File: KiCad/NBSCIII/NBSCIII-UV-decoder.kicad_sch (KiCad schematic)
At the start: 29 parts, among them U2 4053, U3 LM324N

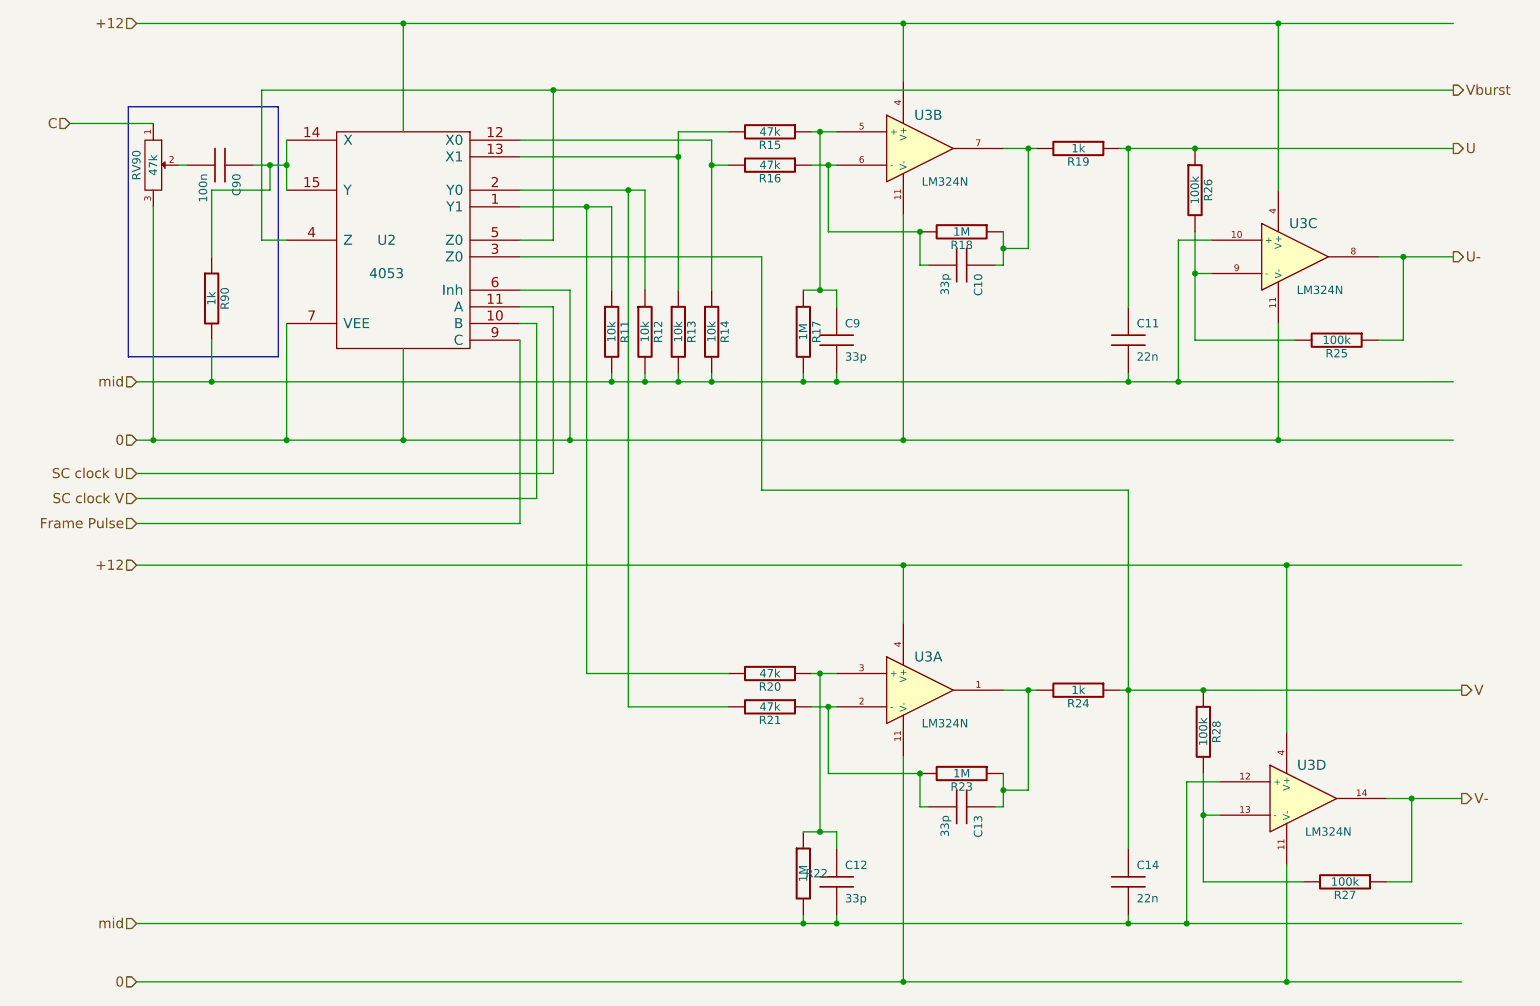
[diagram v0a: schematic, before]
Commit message: unrescue to Device:C
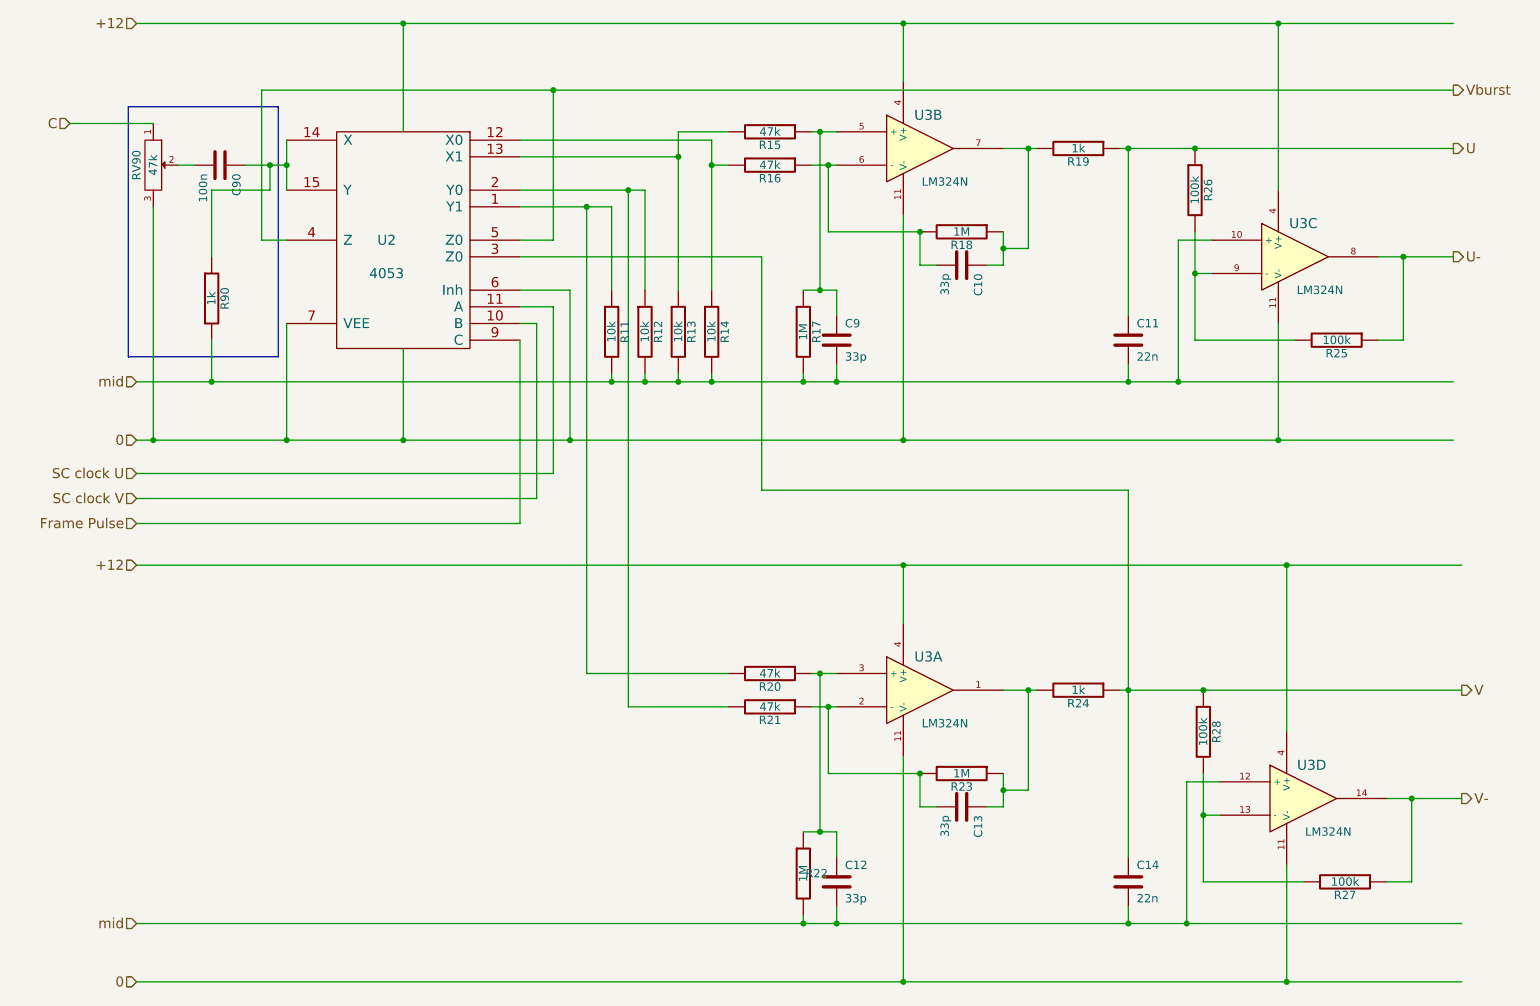
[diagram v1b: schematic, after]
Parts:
- C10, C11, C12, C13, C14, C9, C90: symbol NBSCIII-rescue:C -> Device:C
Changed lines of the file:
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@@
     (stroke (width 0) (type default) (color 0 0 0 0))
   )
-  (wire (pts (xy 41.91 45.72) (xy 40.64 45.72))
+  (wire (pts (xy 40.64 45.72) (xy 43.18 45.72))
     (stroke (width 0) (type default) (color 0 0 0 0))
   )
@@
     (stroke (width 0) (type default) (color 0 0 0 0))
   )
+  (wire (pts (xy 185.42 125.73) (xy 185.42 151.13))
+    (stroke (width 0) (type default) (color 0 0 0 0))
+  )
   (wire (pts (xy 140.97 147.32) (xy 138.43 147.32))
     (stroke (width 0) (type default) (color 0 0 0 0))
@@
     (stroke (width 0) (type default) (color 0 0 0 0))
   )
-  (wire (pts (xy 140.97 67.31) (xy 140.97 64.77))
-    (stroke (width 0) (type default) (color 0 0 0 0))
-  )
   (wire (pts (xy 111.76 49.53) (xy 111.76 64.77))
     (stroke (width 0) (type default) (color 0 0 0 0))
@@
     (stroke (width 0) (type default) (color 0 0 0 0))
   )
-  (wire (pts (xy 165.1 60.96) (xy 166.37 60.96))
+  (wire (pts (xy 185.42 43.18) (xy 185.42 68.58))
+    (stroke (width 0) (type default) (color 0 0 0 0))
+  )
+  (wire (pts (xy 163.83 60.96) (xy 166.37 60.96))
     (stroke (width 0) (type default) (color 0 0 0 0))
   )
@@
     (stroke (width 0) (type default) (color 0 0 0 0))
   )
-  (wire (pts (xy 185.42 67.31) (xy 185.42 43.18))
-    (stroke (width 0) (type default) (color 0 0 0 0))
-  )
   (wire (pts (xy 209.55 152.4) (xy 209.55 170.18))
     (stroke (width 0) (type default) (color 0 0 0 0))
@@
     (stroke (width 0) (type default) (color 0 0 0 0))
   )
-  (wire (pts (xy 165.1 143.51) (xy 166.37 143.51))
+  (wire (pts (xy 163.83 143.51) (xy 166.37 143.51))
     (stroke (width 0) (type default) (color 0 0 0 0))
   )
@@
     (stroke (width 0) (type default) (color 0 0 0 0))
   )
-  (wire (pts (xy 185.42 78.74) (xy 185.42 77.47))
+  (wire (pts (xy 185.42 76.2) (xy 185.42 78.74))
     (stroke (width 0) (type default) (color 0 0 0 0))
   )
@@
     (stroke (width 0) (type default) (color 0 0 0 0))
   )
-  (wire (pts (xy 185.42 161.29) (xy 185.42 160.02))
+  (wire (pts (xy 185.42 158.75) (xy 185.42 161.29))
     (stroke (width 0) (type default) (color 0 0 0 0))
   )
@@
     (stroke (width 0) (type default) (color 0 0 0 0))
   )
+  (wire (pts (xy 140.97 64.77) (xy 140.97 68.58))
+    (stroke (width 0) (type default) (color 0 0 0 0))
+  )
   (wire (pts (xy 236.22 142.24) (xy 228.6 142.24))
     (stroke (width 0) (type default) (color 0 0 0 0))
@@
     (stroke (width 0) (type default) (color 0 0 0 0))
   )
-  (wire (pts (xy 140.97 161.29) (xy 140.97 160.02))
+  (wire (pts (xy 140.97 158.75) (xy 140.97 161.29))
     (stroke (width 0) (type default) (color 0 0 0 0))
   )
@@
     (stroke (width 0) (type default) (color 0 0 0 0))
   )
-  (wire (pts (xy 54.61 45.72) (xy 52.07 45.72))
-    (stroke (width 0) (type default) (color 0 0 0 0))
-  )
-  (wire (pts (xy 185.42 149.86) (xy 185.42 125.73))
+  (wire (pts (xy 50.8 45.72) (xy 54.61 45.72))
     (stroke (width 0) (type default) (color 0 0 0 0))
   )
@@
     (stroke (width 0) (type default) (color 0 0 0 0))
   )
-  (wire (pts (xy 140.97 78.74) (xy 140.97 77.47))
+  (wire (pts (xy 140.97 76.2) (xy 140.97 78.74))
     (stroke (width 0) (type default) (color 0 0 0 0))
   )
@@
     (stroke (width 0) (type default) (color 0 0 0 0))
   )
-  (wire (pts (xy 154.94 60.96) (xy 153.67 60.96))
+  (wire (pts (xy 153.67 60.96) (xy 156.21 60.96))
     (stroke (width 0) (type default) (color 0 0 0 0))
   )
@@
     (stroke (width 0) (type default) (color 0 0 0 0))
   )
-  (wire (pts (xy 140.97 149.86) (xy 140.97 147.32))
+  (wire (pts (xy 140.97 147.32) (xy 140.97 151.13))
     (stroke (width 0) (type default) (color 0 0 0 0))
   )
@@
     (stroke (width 0) (type default) (color 0 0 0 0))
   )
-  (wire (pts (xy 154.94 143.51) (xy 153.67 143.51))
+  (wire (pts (xy 153.67 143.51) (xy 156.21 143.51))
     (stroke (width 0) (type default) (color 0 0 0 0))
   )
@@
     (pin "2")
   )
-  (symbol (lib_id "NBSCIII-rescue:C") (at 140.97 72.39 0) (unit 1)
+  (symbol (lib_id "Device:C") (at 140.97 72.39 0) (unit 1)
     (in_bom yes) (on_board yes)
     (property "Reference" "C9" (id 0) (at 142.24 69.85 0)
@@
     (pin "2")
   )
-  (symbol (lib_id "NBSCIII-rescue:C") (at 160.02 60.96 270) (unit 1)
+  (symbol (lib_id "Device:C") (at 160.02 60.96 270) (unit 1)
     (in_bom yes) (on_board yes)
     (property "Reference" "C10" (id 0) (at 162.56 62.23 0)
@@
     (pin "2")
   )
-  (symbol (lib_id "NBSCIII-rescue:C") (at 185.42 72.39 0) (unit 1)
+  (symbol (lib_id "Device:C") (at 185.42 72.39 0) (unit 1)
     (in_bom yes) (on_board yes)
     (property "Reference" "C11" (id 0) (at 186.69 69.85 0)
@@
     (pin "2")
   )
-  (symbol (lib_id "NBSCIII-rescue:C") (at 140.97 154.94 0) (unit 1)
+  (symbol (lib_id "Device:C") (at 140.97 154.94 0) (unit 1)
     (in_bom yes) (on_board yes)
     (property "Reference" "C12" (id 0) (at 142.24 152.4 0)
@@
     (pin "2")
   )
-  (symbol (lib_id "NBSCIII-rescue:C") (at 160.02 143.51 270) (unit 1)
+  (symbol (lib_id "Device:C") (at 160.02 143.51 270) (unit 1)
     (in_bom yes) (on_board yes)
     (property "Reference" "C13" (id 0) (at 162.56 144.78 0)
@@
     (pin "2")
   )
-  (symbol (lib_id "NBSCIII-rescue:C") (at 185.42 154.94 0) (unit 1)
+  (symbol (lib_id "Device:C") (at 185.42 154.94 0) (unit 1)
     (in_bom yes) (on_board yes)
     (property "Reference" "C14" (id 0) (at 186.69 152.4 0)
@@
     (pin "3")
   )
-  (symbol (lib_id "NBSCIII-rescue:C") (at 46.99 45.72 270) (unit 1)
+  (symbol (lib_id "Device:C") (at 46.99 45.72 270) (unit 1)
     (in_bom yes) (on_board yes)
     (property "Reference" "C90" (id 0) (at 49.53 46.99 0)

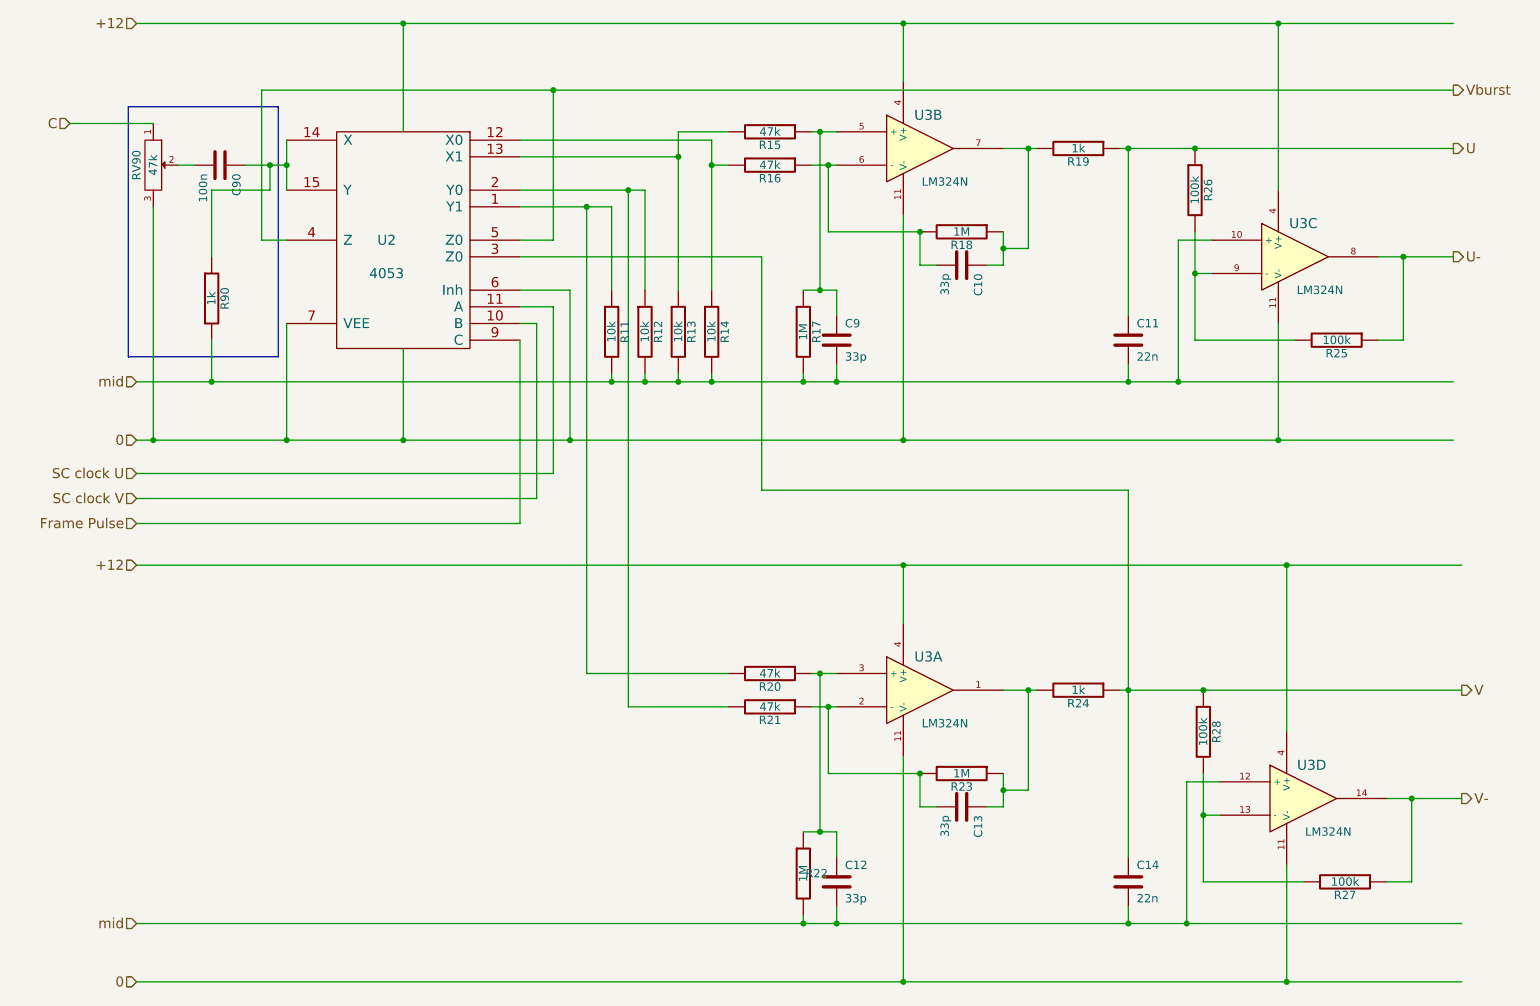
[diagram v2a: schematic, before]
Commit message: unrescue Device:R
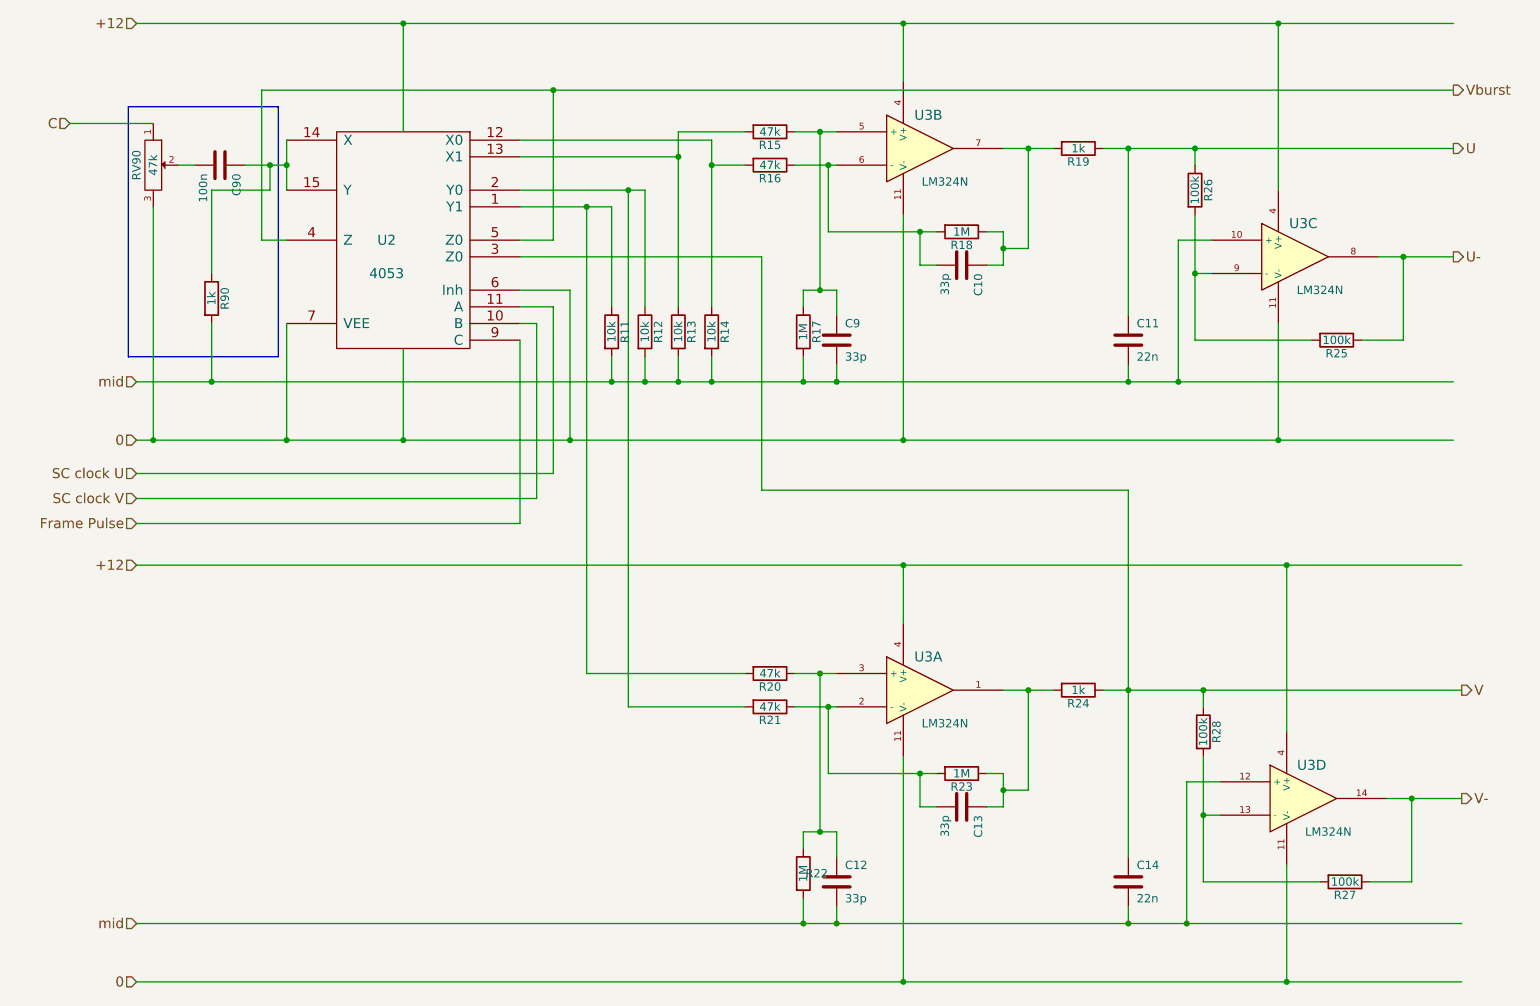
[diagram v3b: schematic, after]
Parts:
- R11, R12, R13, R14, R15, R16, R17, R18, R19, R20, R21, R22, R23, R24, R25, R26, R27, R28, R90: symbol NBSCIII-rescue:R -> Device:R

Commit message: unrescue Device:R_potentiometer
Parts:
- RV90: symbol NBSCIII-rescue:POT -> Device:R_Potentiometer
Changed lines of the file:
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@@
+    (stroke (width 0) (type default) (color 0 0 0 0))
+  )
+  (wire (pts (xy 36.83 39.37) (xy 36.83 41.91))
     (stroke (width 0) (type default) (color 0 0 0 0))
   )
@@
     (stroke (width 0) (type default) (color 0 0 0 0))
   )
-  (wire (pts (xy 36.83 52.07) (xy 36.83 87.63))
+  (wire (pts (xy 36.83 49.53) (xy 36.83 87.63))
     (stroke (width 0) (type default) (color 0 0 0 0))
   )
@@
     (pin "2")
   )
-  (symbol (lib_id "NBSCIII-rescue:POT") (at 36.83 45.72 270) (unit 1)
-    (in_bom yes) (on_board yes)
-    (property "Reference" "RV90" (id 0) (at 34.29 45.72 0))
-    (property "Value" "47k" (id 1) (at 36.83 45.72 0))
+  (symbol (lib_id "Device:R_Potentiometer") (at 36.83 45.72 0) (unit 1)
+    (in_bom yes) (on_board yes)
+    (property "Reference" "RV90" (id 0) (at 33.02 49.53 0))
+    (property "Value" "47k" (id 1) (at 36.83 45.72 90))
     (property "Footprint" "" (id 2) (at 36.83 45.72 0)
       (effects (font (size 1.27 1.27)) hide)
